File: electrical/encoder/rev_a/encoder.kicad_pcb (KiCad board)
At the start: 2 copper layers, 14.8 x 40.4 mm, 5 parts, among them CN1 ENCODER;2xM1x3RA, Q1 AH1806;SC59, Q2 AH1806;SC59

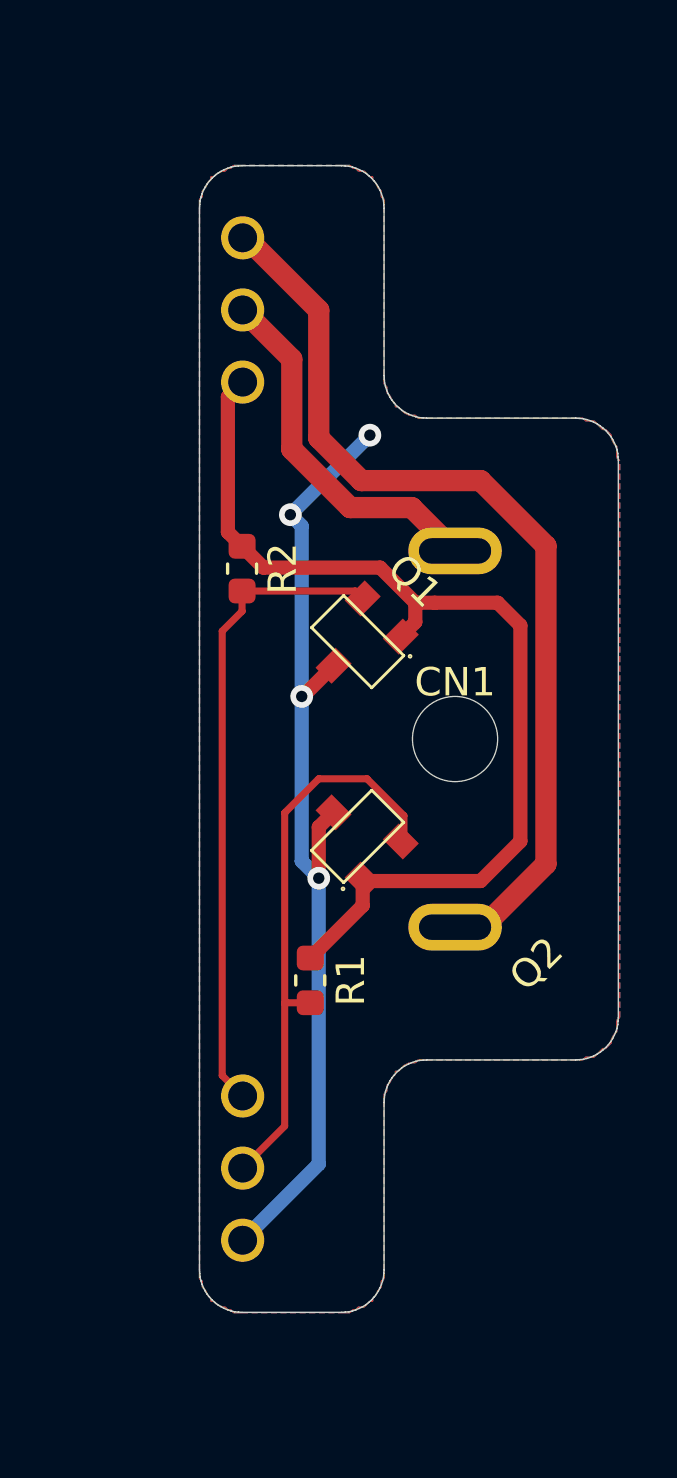
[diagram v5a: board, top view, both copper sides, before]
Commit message: Moved Encoder connectors out by .127mm.
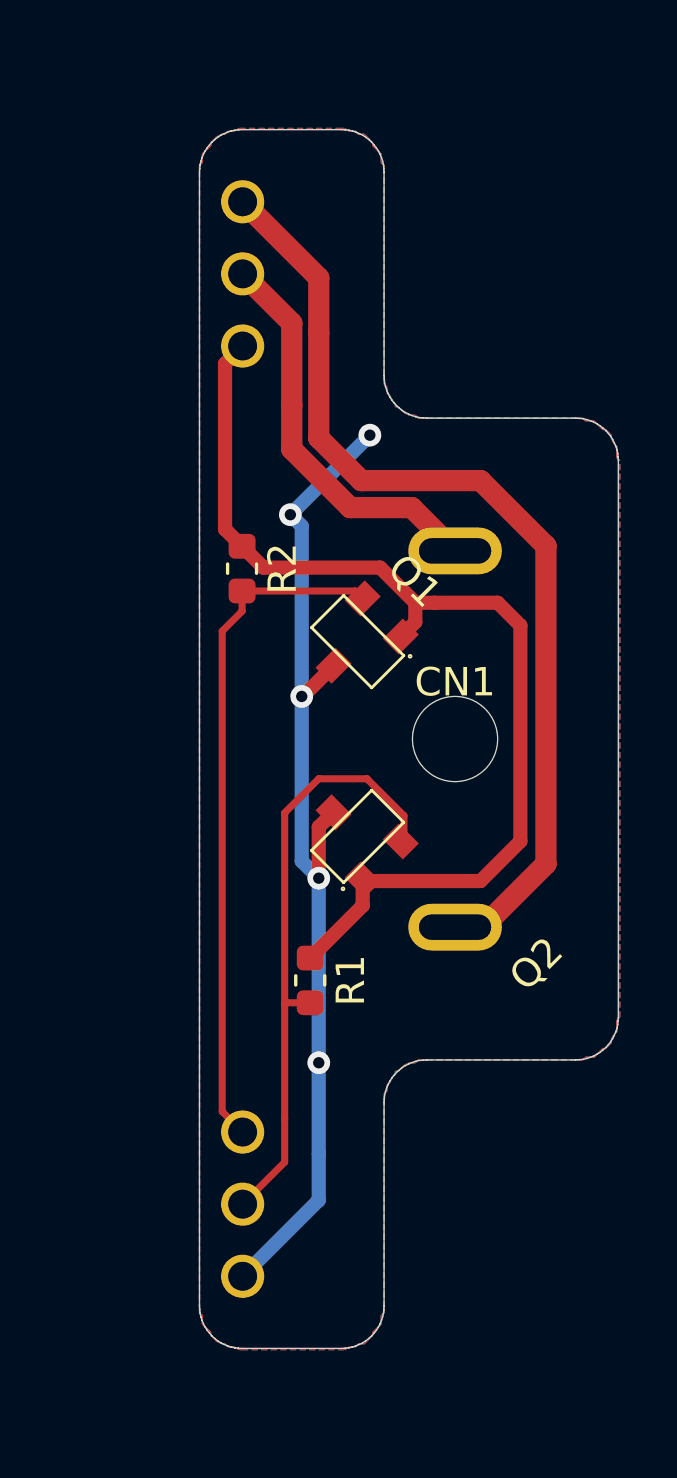
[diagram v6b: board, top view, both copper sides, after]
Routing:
- net /VCC: track 35.8 -> 37.2 mm
- net /QUADB: track 22.7 -> 24.0 mm
- net /GND: track 35.1 -> 36.4 mm, vias 4 -> 5
- net /QUADA: track 20.2 -> 21.5 mm
- net /MOTOR+: track 12.9 -> 14.1 mm
- net /MOTOR-: track 33.1 -> 34.3 mm
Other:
- board size 14.8 x 40.4 mm -> 14.8 x 42.9 mm

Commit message: Lots of work on the PCB.
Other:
- board size 14.8 x 42.9 mm -> 14.8 x 48 mm
